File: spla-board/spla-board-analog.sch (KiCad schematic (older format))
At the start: 38 parts, among them J13 J_ANALOG, J14 J_AREF, U4 ADC1173, U5 ADC1173, U6 ADC1173

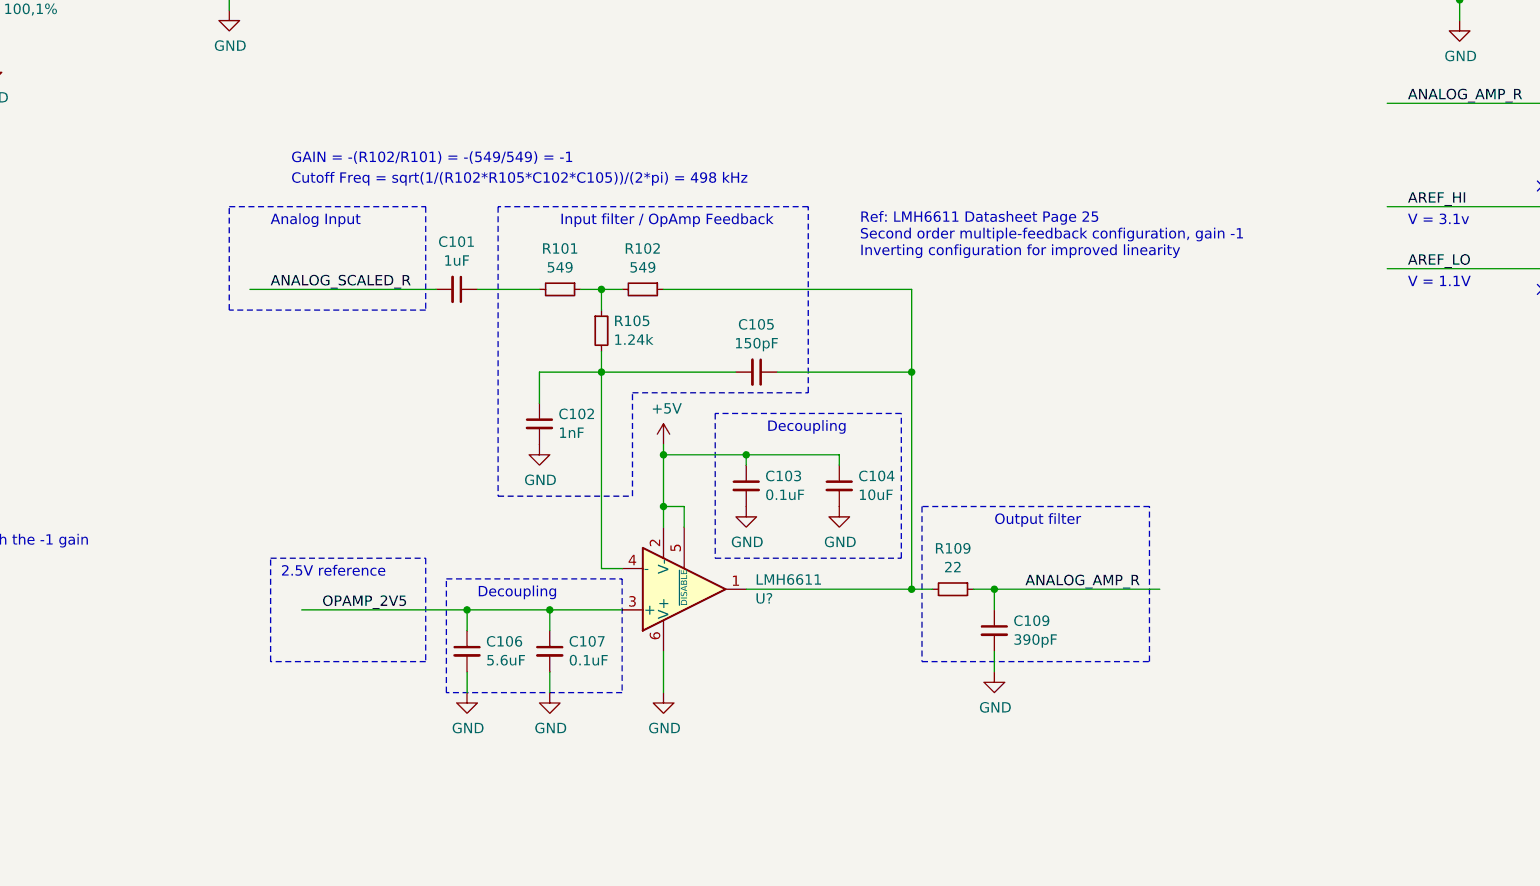
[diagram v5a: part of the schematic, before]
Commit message: schematic: Fix analog values for 50MHz filter; correct symbol orientation.
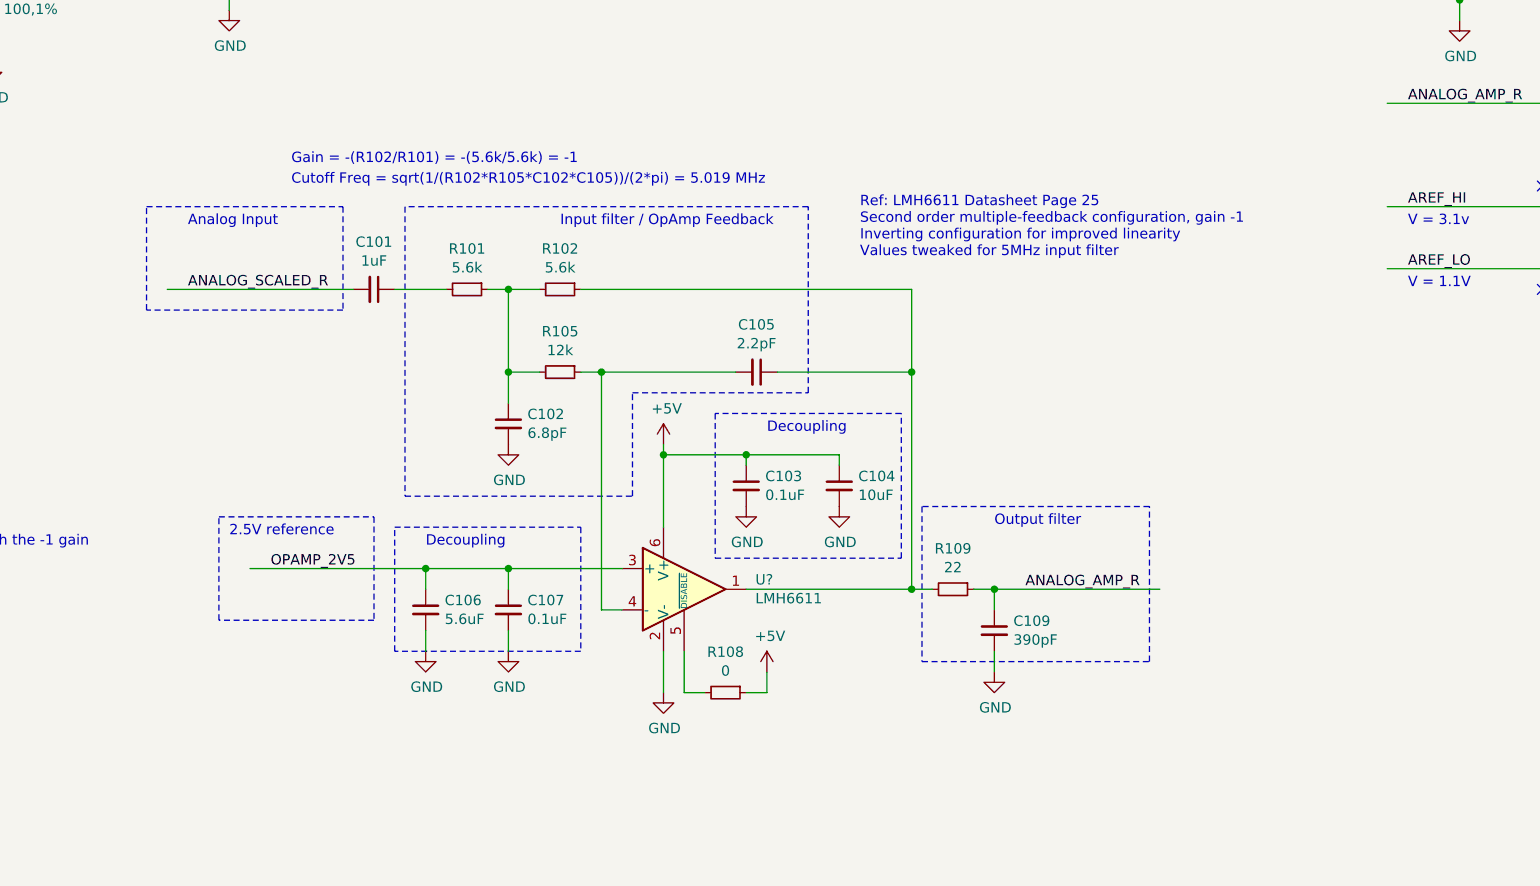
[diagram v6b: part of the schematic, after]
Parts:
- added R108: 0, symbol Device:R_Small
- C102: value 1nF -> 6.8pF
- C105: value 150pF -> 2.2pF
- R101, R102: value 549 -> 5.6k
- R105: value 1.24k -> 12k
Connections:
- wire segments 144 -> 145
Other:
- note added: "Cutoff Freq = sqrt(1/(R102*R105*C102*C105))/(2*pi) = 5.019 MHz"
- note added: "Gain = -(R102/R101) = -(5.6k/5.6k) = -1"
- note added: "Ref: LMH6611 Datasheet Page 25\nSecond order multiple-feedback configuration, gain -1\nInverting configuration for improved linearity\nValues tweaked for 5MHz input filter"
- note removed: "Cutoff Freq = sqrt(1/(R102*R105*C102*C105))/(2*pi) = 498 kHz"
- note removed: "GAIN = -(R102/R101) = -(549/549) = -1"
- note removed: "Ref: LMH6611 Datasheet Page 25\nSecond order multiple-feedback configuration, gain -1\nInverting configuration for improved linearity"
- moved on the sheet: C101, C102, C106, C107, R101, R102, R105
